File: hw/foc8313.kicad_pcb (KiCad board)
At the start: 4 copper layers, 35 x 35 mm, 162 parts, among them J1 Tag Connect, J2 Encoder, J3 CAN, J4 CAN, J6 GPIO, SW1 SW_SPST, SW2 SW_SPST, U1 LMR36015SFBRNXR, U10 ISO6521F, U12 TJA1051TK/3,118, U2 XC6206P332MR, U3 DRV8313PWP, U4 STM32F103CBTx, U5 AS5047D, U6 ZD24C08AE1-STGMT, U7 INA240A2D, U8 INA240A2D, X1 X322516MLB4SI

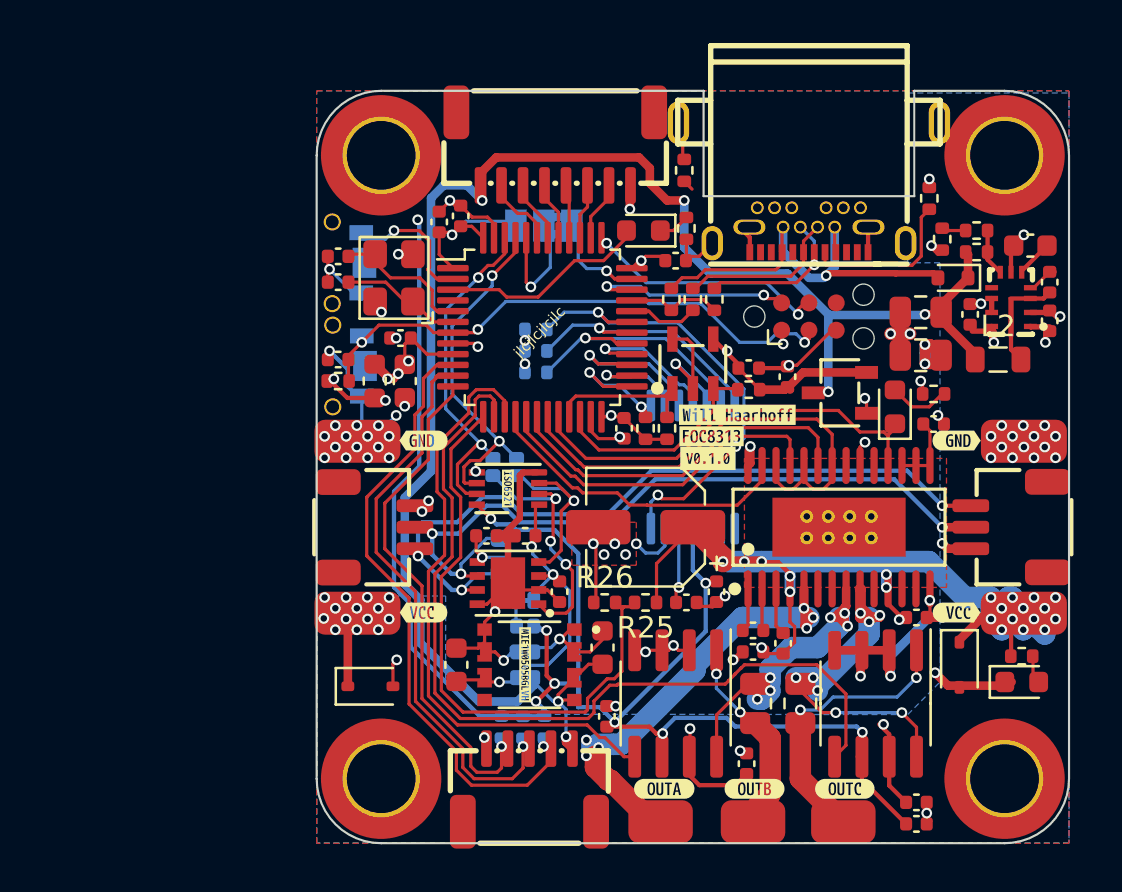
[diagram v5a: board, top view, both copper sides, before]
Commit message: [Hw] Plane geometry changes, more legible silkscreen
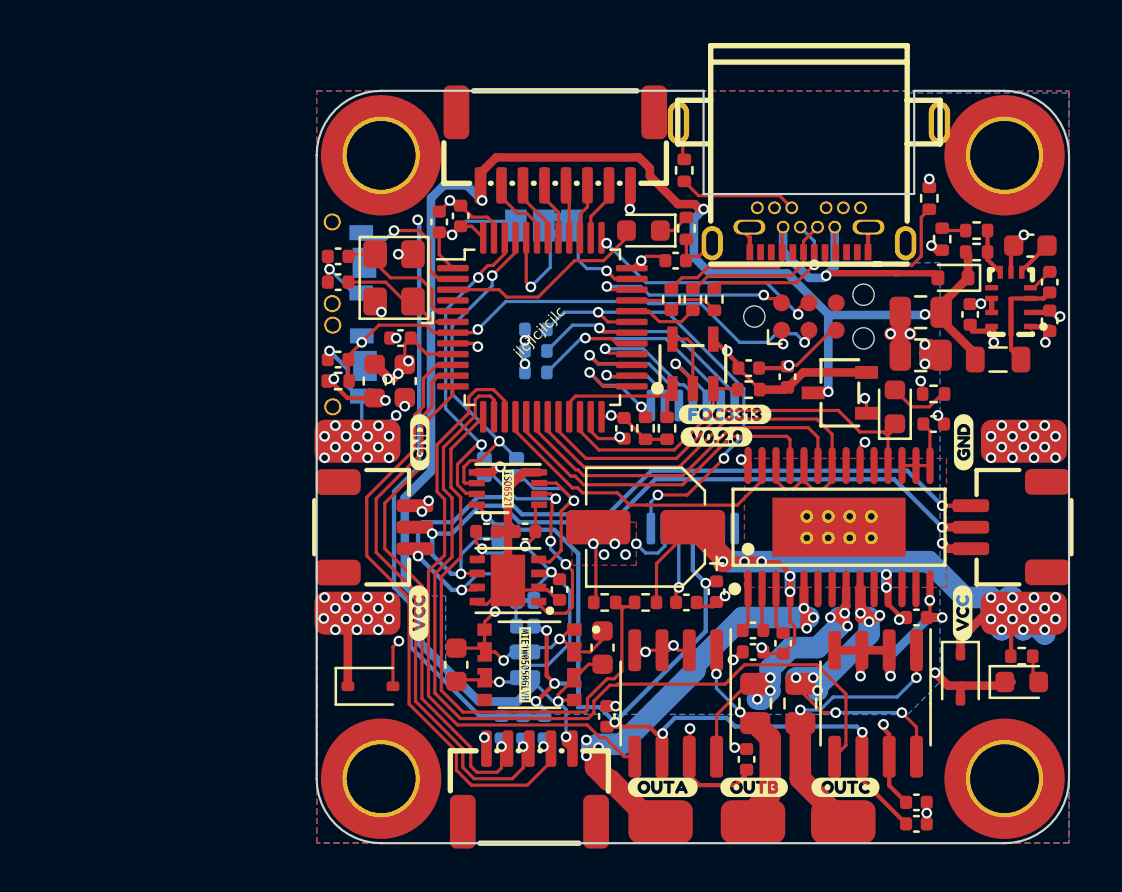
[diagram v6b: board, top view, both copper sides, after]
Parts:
- removed kibuzzard-6635905B: G***, kibuzzard-6635905B
- removed kibuzzard-6635906D: G***, kibuzzard-6635906D
- removed kibuzzard-66359090: G***, kibuzzard-66359090
- removed kibuzzard-663591A5: G***, kibuzzard-663591A5
- removed kibuzzard-663591BC: G***, kibuzzard-663591BC
- removed kibuzzard-663591C6: G***, kibuzzard-663591C6
- removed kibuzzard-6635923C (x4): G***, kibuzzard-6635923C
- removed kibuzzard-6635926F: G***, kibuzzard-6635926F
- removed kibuzzard-66359297 (x2): G***, kibuzzard-66359297
- removed kibuzzard-663592D6 (x3): G***, kibuzzard-663592D6
- removed kibuzzard-66359322: G***, kibuzzard-66359322
- removed kibuzzard-66359333: G***, kibuzzard-66359333
- removed kibuzzard-6635934E: G***, kibuzzard-6635934E
- removed kibuzzard-66359356: G***, kibuzzard-66359356
- removed kibuzzard-6635935F: G***, kibuzzard-6635935F
- removed kibuzzard-66359375: G***, kibuzzard-66359375
- removed kibuzzard-6635961B: G***, kibuzzard-6635961B
- removed kibuzzard-66359642: G***, kibuzzard-66359642
- removed kibuzzard-663596D7: G***, kibuzzard-663596D7
- removed kibuzzard-66359707: G***, kibuzzard-66359707
- removed kibuzzard-6635971B: G***, kibuzzard-6635971B
- removed kibuzzard-6635973B: G***, kibuzzard-6635973B
- removed kibuzzard-6635974A: G***, kibuzzard-6635974A
- removed kibuzzard-66359780 (x2): G***, kibuzzard-66359780
- removed kibuzzard-66359792: G***, kibuzzard-66359792
- removed kibuzzard-663597E2: G***, kibuzzard-663597E2
- removed kibuzzard-6635988E: G***, kibuzzard-6635988E
- removed kibuzzard-663598FD: G***, kibuzzard-663598FD
- removed kibuzzard-663599A9: G***, kibuzzard-663599A9
- removed kibuzzard-663599B0: G***, kibuzzard-663599B0
- removed kibuzzard-66359A05: G***, kibuzzard-66359A05
- removed kibuzzard-66359A1C: G***, kibuzzard-66359A1C
- removed kibuzzard-66359A28: G***, kibuzzard-66359A28
- removed kibuzzard-66359A50: G***, kibuzzard-66359A50
- removed kibuzzard-66359A77: G***, kibuzzard-66359A77
- removed kibuzzard-66359A9E: G***, kibuzzard-66359A9E
- removed kibuzzard-66359AB0: G***, kibuzzard-66359AB0
- removed kibuzzard-66359AE4: G***, kibuzzard-66359AE4
- removed kibuzzard-66359B17: G***, kibuzzard-66359B17
- removed kibuzzard-6635FB63: G***, kibuzzard-6635FB63
- removed kibuzzard-6635FB77: G***, kibuzzard-6635FB77
- removed kibuzzard-6635FB7E: G***, kibuzzard-6635FB7E
- removed kibuzzard-6635FC0D (x2): G***, kibuzzard-6635FC0D
- removed kibuzzard-6635FC16 (x2): G***, kibuzzard-6635FC16
- removed kibuzzard-667F5C34: G***, kibuzzard-667F5C34
- added kibuzzard-6687B916: G***, kibuzzard-6687B916, B.Cu at (134.3, 91.3)
- added kibuzzard-6687B916: G***, kibuzzard-6687B916, B.Cu at (137.2, 84.2)
- added kibuzzard-6687B916: G***, kibuzzard-6687B916, B.Cu at (130.3, 115.8)
- added kibuzzard-6687B916: G***, kibuzzard-6687B916, B.Cu at (135.1, 108.6)
- added kibuzzard-6687B962: G***, kibuzzard-6687B962, B.Cu at (136.2, 84.2)
- added kibuzzard-6687B96D: G***, kibuzzard-6687B96D, B.Cu at (135.2, 84.1)
- added kibuzzard-6687B975: G***, kibuzzard-6687B975, B.Cu at (134.1, 84.1)
- added kibuzzard-6687B97C: G***, kibuzzard-6687B97C, B.Cu at (133.1, 84.1)
- added kibuzzard-6687B983: G***, kibuzzard-6687B983, B.Cu at (132.0, 84.0)
- added kibuzzard-6687B989: G***, kibuzzard-6687B989, B.Cu at (130.9, 84.1)
- added kibuzzard-6687B990: G***, kibuzzard-6687B990, B.Cu at (129.9, 83.9)
- added kibuzzard-6687B990: G***, kibuzzard-6687B990, B.Cu at (134.5, 116.2)
- added kibuzzard-6687BB13: G***, kibuzzard-6687BB13, B.Cu at (133.1, 91.8)
- added kibuzzard-6687BB22: G***, kibuzzard-6687BB22, B.Cu at (131.8, 91.2)
- added kibuzzard-6687BB56: G***, kibuzzard-6687BB56, B.Cu at (128.0, 90.0)
- added kibuzzard-6687BB64: G***, kibuzzard-6687BB64, B.Cu at (128.1, 95.8)
- added kibuzzard-6687BBB1: G***, kibuzzard-6687BBB1, B.Cu at (131.3, 115.8)
- added kibuzzard-6687BBBA: G***, kibuzzard-6687BBBA, B.Cu at (132.4, 115.7)
- added kibuzzard-6687BBC5: G***, kibuzzard-6687BBC5, B.Cu at (133.4, 115.7)
- added kibuzzard-6687BC5B: G***, kibuzzard-6687BC5B, B.Cu at (138.4, 115.5)
- added kibuzzard-6687BC64: G***, kibuzzard-6687BC64, B.Cu at (142.7, 115.6)
- added kibuzzard-6687BC6D: G***, kibuzzard-6687BC6D, B.Cu at (147.1, 115.6)
- added kibuzzard-6687BCF3: G***, kibuzzard-6687BCF3, B.Cu at (124.3, 100.5)
- added kibuzzard-6687BCF3: G***, kibuzzard-6687BCF3, B.Cu at (155.8, 100.5)
- added kibuzzard-6687BD2B: G***, kibuzzard-6687BD2B, B.Cu at (155.8, 105.0)
- added kibuzzard-6687BD2B: G***, kibuzzard-6687BD2B, B.Cu at (124.3, 105.0)
- added kibuzzard-6687BD69: G***, kibuzzard-6687BD69, B.Cu at (125.0, 101.7)
- added kibuzzard-6687BD70: G***, kibuzzard-6687BD70, B.Cu at (124.3, 102.8)
- added kibuzzard-6687BD76: G***, kibuzzard-6687BD76, B.Cu at (124.4, 103.9)
- added kibuzzard-6687BD8E: G***, kibuzzard-6687BD8E, B.Cu at (128.7, 108.6)
- added kibuzzard-6687BD8E: G***, kibuzzard-6687BD8E, B.Cu at (155.1, 103.9)
- added kibuzzard-6687BD97: G***, kibuzzard-6687BD97, B.Cu at (155.7, 102.8)
- added kibuzzard-6687BD9D: G***, kibuzzard-6687BD9D, B.Cu at (155.7, 101.7)
- added kibuzzard-6687BF56: G***, kibuzzard-6687BF56, B.Cu at (134.4, 99.5)
- added kibuzzard-6687BF5D: G***, kibuzzard-6687BF5D, B.Cu at (134.2, 100.5)
- added kibuzzard-6687BFAE: G***, kibuzzard-6687BFAE, B.Cu at (135.3, 106.2)
- added kibuzzard-6687BFB6: G***, kibuzzard-6687BFB6, B.Cu at (135.0, 107.4)
- added kibuzzard-6687BFD2: G***, kibuzzard-6687BFD2, B.Cu at (134.7, 109.8)
- added kibuzzard-6687BFE6: G***, kibuzzard-6687BFE6, B.Cu at (129.2, 109.8)
- added kibuzzard-6687C00C: G***, kibuzzard-6687C00C, B.Cu at (129.1, 107.5)
- added kibuzzard-6687C00C: G***, kibuzzard-6687C00C, B.Cu at (129.1, 106.2)
- added kibuzzard-6687C0E6: G***, kibuzzard-6687C0E6, B.Cu at (132.8, 103.9)
- added kibuzzard-6687C12A: G***, kibuzzard-6687C12A, B.Cu at (127.9, 100.5)
- added kibuzzard-6687C148: G***, kibuzzard-6687C148, B.Cu at (127.9, 99.5)
- added kibuzzard-6687C371: G***, kibuzzard-6687C371, F.Cu at (152.6, 98.8)
- added kibuzzard-6687C371: G***, kibuzzard-6687C371, F.Cu at (127.3, 98.8)
- added kibuzzard-6687C3AC: G***, kibuzzard-6687C3AC, F.Cu at (127.2, 106.8)
- added kibuzzard-6687C3AC: G***, kibuzzard-6687C3AC, F.Cu at (152.6, 106.8)
- added kibuzzard-6687C408: G***, kibuzzard-6687C408, F.Cu at (147.1, 114.9)
- added kibuzzard-6687C440: G***, kibuzzard-6687C440, F.Cu at (142.8, 114.9)
- added kibuzzard-6687C487: G***, kibuzzard-6687C487, F.Cu at (138.6, 114.9)
- added kibuzzard-6687C4B0: G***, kibuzzard-6687C4B0, F.Cu at (141.5, 97.5)
- added kibuzzard-6687C4F0: G***, kibuzzard-6687C4F0, F.Cu at (141.1, 98.6)
- moved D1 0.55 mm to (152.4, 109.8)
- moved JP6 0.40 mm to (130.3, 100.0)
- moved C29 0.20 mm to (142.5, 113.6)
- moved C34 0.20 mm to (130.4, 103.0)
- moved C35 0.20 mm to (132.2, 103.0)
- moved U12 0.12 mm to (131.4, 105.3)
- moved C33 0.10 mm to (133.8, 105.7)
- moved R2 0.06 mm to (131.1, 104.2)
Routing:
- net Net-(USB1-CC2): track 0.52 -> 5.51 mm
- net GND: track 93.6 -> 96.3 mm
- net /CAN.GND: track 21.4 -> 23.3 mm
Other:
- outline, holes or cut-outs redrawn
- board text added: "V0.2.0"
- board text removed: "Version 0.1.0"
